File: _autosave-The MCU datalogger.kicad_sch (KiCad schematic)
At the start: 21 parts, among them U1 24LC1025, U2 DS1337S+, U3 24LC1025, U4 ATMEGA328P-AU, Y1 32.768 KHz, Y2 16 MHz

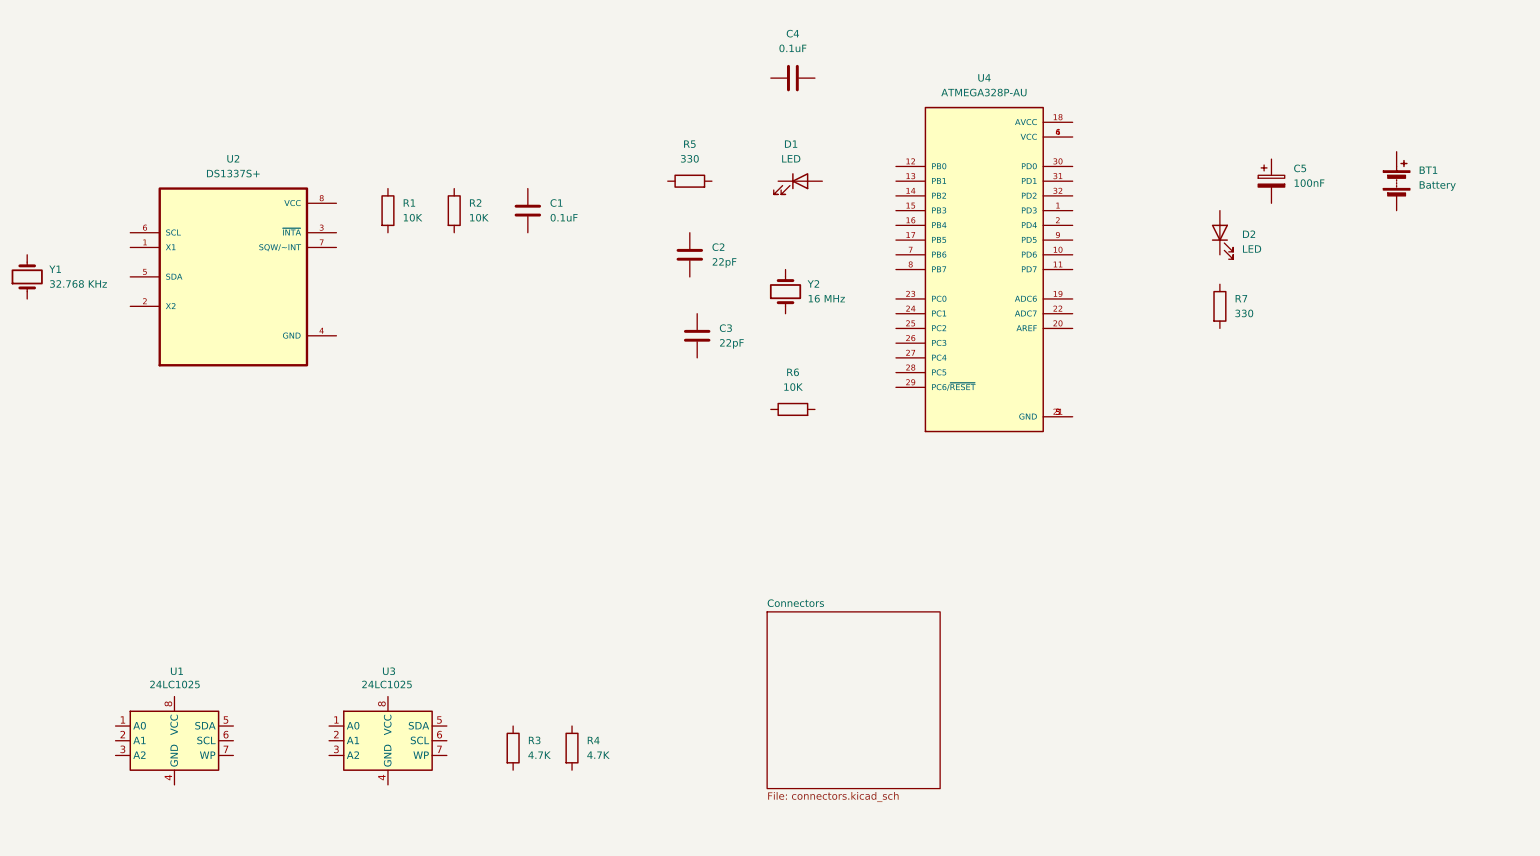
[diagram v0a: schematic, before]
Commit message: Completed wiring of main sheet.
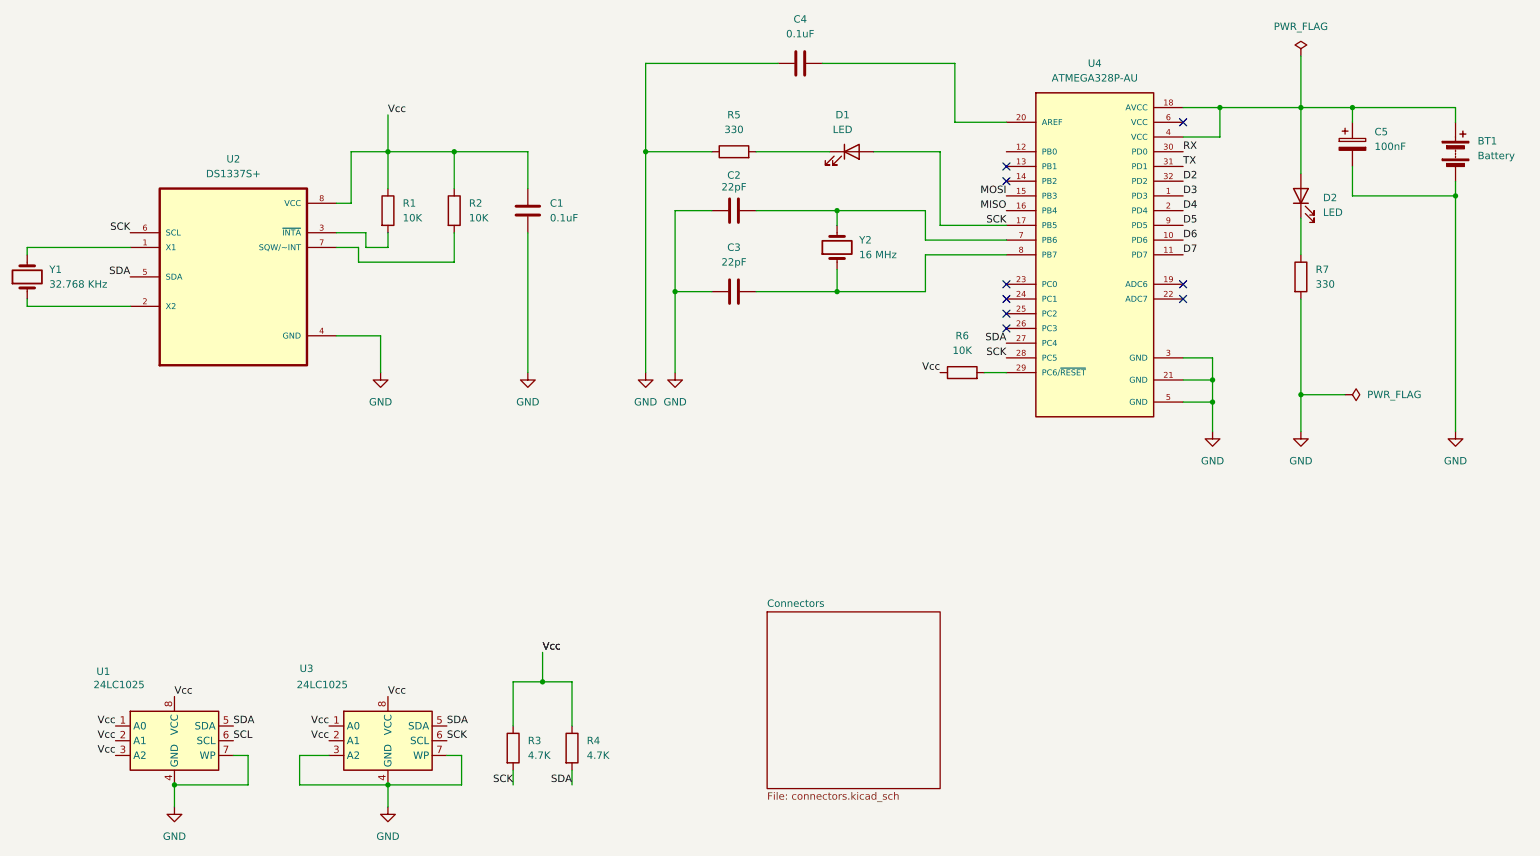
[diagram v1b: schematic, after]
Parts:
- U4: MF Microchip Technology -> (none)
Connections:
- net Vcc: now reaches U3.1 (A0)
- net Vcc: now also C1.1, R1.1, R2.1, R3.1, R4.1, R6.1, U1.1 (A0), U1.2 (A1), U1.3 (A2), U1.8 (VCC), U2.8 (VCC), U3.2 (A1), U3.8 (VCC)
- net GND: now reaches U3.3 (A2)
- net GND: now also BT1.2 (-), C1.2, C2.2, C3.2, C4.1, C5.2, R5.1, R7.2, U1.4 (GND), U1.7 (WP), U2.4 (GND), U3.4 (GND), U3.7 (WP), U4.21 (GND), U4.3 (GND), U4.5 (GND)
- net SDA: now reaches U3.5 (SDA)
- net SDA: now also R4.2, U1.5 (SDA), U2.5 (SDA), U4.27 (PC4)
- net SCK: now reaches U3.6 (SCL)
- net SCK: now also D1.2 (A), R3.2, U2.6 (SCL), U4.17 (PB5), U4.28 (PC5)
- net at Y1.1: now also U2.2 (X2)
- net at Y1.2: now also U2.1 (X1)
- net at BT1.1 (+): now also C5.1, D2.2 (A), U4.18 (AVCC), U4.4 (VCC)
- net at R5.2: now also D1.1 (K)
- net at R1.2: now also U2.3 (~{INTA})
- net at R6.2: now also U4.29 (PC6/~{RESET})
- net at C4.2: now also U4.20 (AREF)
- net at R7.1: now also D2.1 (K)
- net at R2.2: now also U2.7 (SQW/~INT)
- net SCL: now reaches U1.6 (SCL)
- net at C2.1: now also U4.7 (PB6), Y2.2
- net D3: now reaches U4.1 (PD3)
- net D6: now reaches U4.10 (PD6)
- net D7: now reaches U4.11 (PD7)
- net MOSI: now reaches U4.15 (PB3)
- net MISO: now reaches U4.16 (PB4)
- net D4: now reaches U4.2 (PD4)
- net RX: now reaches U4.30 (PD0)
- net TX: now reaches U4.31 (PD1)
- net D2: now reaches U4.32 (PD2)
- net at U4.6 (VCC): no longer U4.4 (VCC)
- net at U4.8 (PB7): now also C3.1, Y2.1
- net D5: now reaches U4.9 (PD5)
- no-connect marks 0 -> 9
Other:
- moved on the sheet: BT1, C2, C3, C4, C5, D1, D2, R5, R6, R7, Y2
